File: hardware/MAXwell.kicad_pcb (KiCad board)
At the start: 2 copper layers, 155 parts, among them J1 Conn_02x05_Odd_Even, J2 Conn_02x12_Counter_Clockwise, J3 Barrel_Jack_Switch_Pin3Ring, SW1 SW_Push_Dual, SW10 SW_Wuerth_450301014042, SW11 SW_Wuerth_450301014042, SW12 SW_Wuerth_450301014042, SW13 SW_Wuerth_450301014042, SW2 SW_Push_Dual, SW3 SW_Push_Dual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

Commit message: started routing
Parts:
- SW1, SW2, SW3, SW4: footprint Button_Switch_THT:SW_PUSH-12mm -> Library:SW_PUSH-12mm
- moved D1 125.7 mm to (236.7, 131.5)
- moved D14 125.7 mm to (246.3, 134.5)
- moved D15 125.7 mm to (246.3, 137.5)
- moved D16 125.7 mm to (246.3, 140.6)
- moved D2 125.7 mm to (236.7, 134.5)
- moved D3 125.7 mm to (236.7, 137.5)
- moved D4 125.7 mm to (236.7, 140.6)
- moved D5 125.7 mm to (236.7, 143.6)
- moved R1 125.4 mm to (260.4, 109.3)
- moved R2 125.4 mm to (260.4, 112.2)
- moved R3 125.4 mm to (260.4, 115.2)
- moved R5 125.4 mm to (260.4, 121.1)
- moved R4 125.4 mm to (260.4, 118.1)
- moved R62 116.8 mm to (273.8, 128.0)
- moved R63 116.8 mm to (273.8, 130.9)
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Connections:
- J2 pad 2: +3V3 -> GND
- J2 pad 21: GND -> Net-(J2-Pin_21)
- J2 pad 22: GND -> Net-(J2-Pin_22)
- J2 pad 23: GND -> Net-(J2-Pin_23)
- J2 pad 24: GND -> Net-(J2-Pin_24)
- J2 pad 3: Net-(J2-Pin_3) -> +3V3
- J2 pad 4: Net-(J2-Pin_4) -> GND
- J2 pad 6: Net-(J2-Pin_6) -> GND
- J2 pad 8: Net-(J2-Pin_8) -> GND
- U5 pad 62: Net-(J2-Pin_3) -> Net-(J2-Pin_5)
- U5 pad 64: Net-(J2-Pin_4) -> Net-(J2-Pin_7)
- U5 pad 66: Net-(J2-Pin_5) -> Net-(J2-Pin_9)
- U5 pad 67: Net-(J2-Pin_6) -> Net-(J2-Pin_11)
- U5 pad 68: Net-(J2-Pin_7) -> Net-(J2-Pin_13)
- U5 pad 69: Net-(J2-Pin_8) -> Net-(J2-Pin_15)
- U5 pad 70: Net-(J2-Pin_9) -> Net-(J2-Pin_17)
- U5 pad 71: Net-(J2-Pin_10) -> Net-(J2-Pin_19)
- U5 pad 72: Net-(J2-Pin_11) -> Net-(J2-Pin_21)
- U5 pad 73: Net-(J2-Pin_12) -> Net-(J2-Pin_23)
- U5 pad 74: Net-(J2-Pin_13) -> Net-(J2-Pin_24)
- U5 pad 75: Net-(J2-Pin_14) -> Net-(J2-Pin_22)
- U5 pad 76: Net-(J2-Pin_15) -> Net-(J2-Pin_20)
- U5 pad 77: Net-(J2-Pin_16) -> Net-(J2-Pin_18)
- U5 pad 78: Net-(J2-Pin_17) -> Net-(J2-Pin_16)
- U5 pad 81: Net-(J2-Pin_18) -> Net-(J2-Pin_14)
- U5 pad 82: Net-(J2-Pin_19) -> Net-(J2-Pin_12)
- U5 pad 83: Net-(J2-Pin_20) -> Net-(J2-Pin_10)
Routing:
- net +3V3: track 0.00 -> 110.3 mm
- net Net-(R45-Pad2): track 0.00 -> 18.3 mm
- net Net-(R50-Pad2): track 0.00 -> 18.3 mm
- net Net-(R42-Pad2): track 0.00 -> 18.2 mm
- net Net-(R48-Pad2): track 0.00 -> 18.2 mm
- net Net-(U5-IO1_12/GCLK0): track 0.00 -> 17.1 mm
- net Net-(R47-Pad1): track 0.00 -> 16.7 mm
- net Net-(R44-Pad1): track 0.00 -> 16.7 mm
- net Net-(R61-Pad1): track 0.00 -> 16.6 mm
- net Net-(R60-Pad1): track 0.00 -> 16.6 mm
- net Net-(SW11-C): track 0.00 -> 13.5 mm
- net Net-(SW10-C): track 0.00 -> 13.5 mm
- net Net-(SW8-C): track 0.00 -> 13.5 mm
- net Net-(SW7-C): track 0.00 -> 13.5 mm
- net Net-(SW6-C): track 0.00 -> 13.5 mm
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
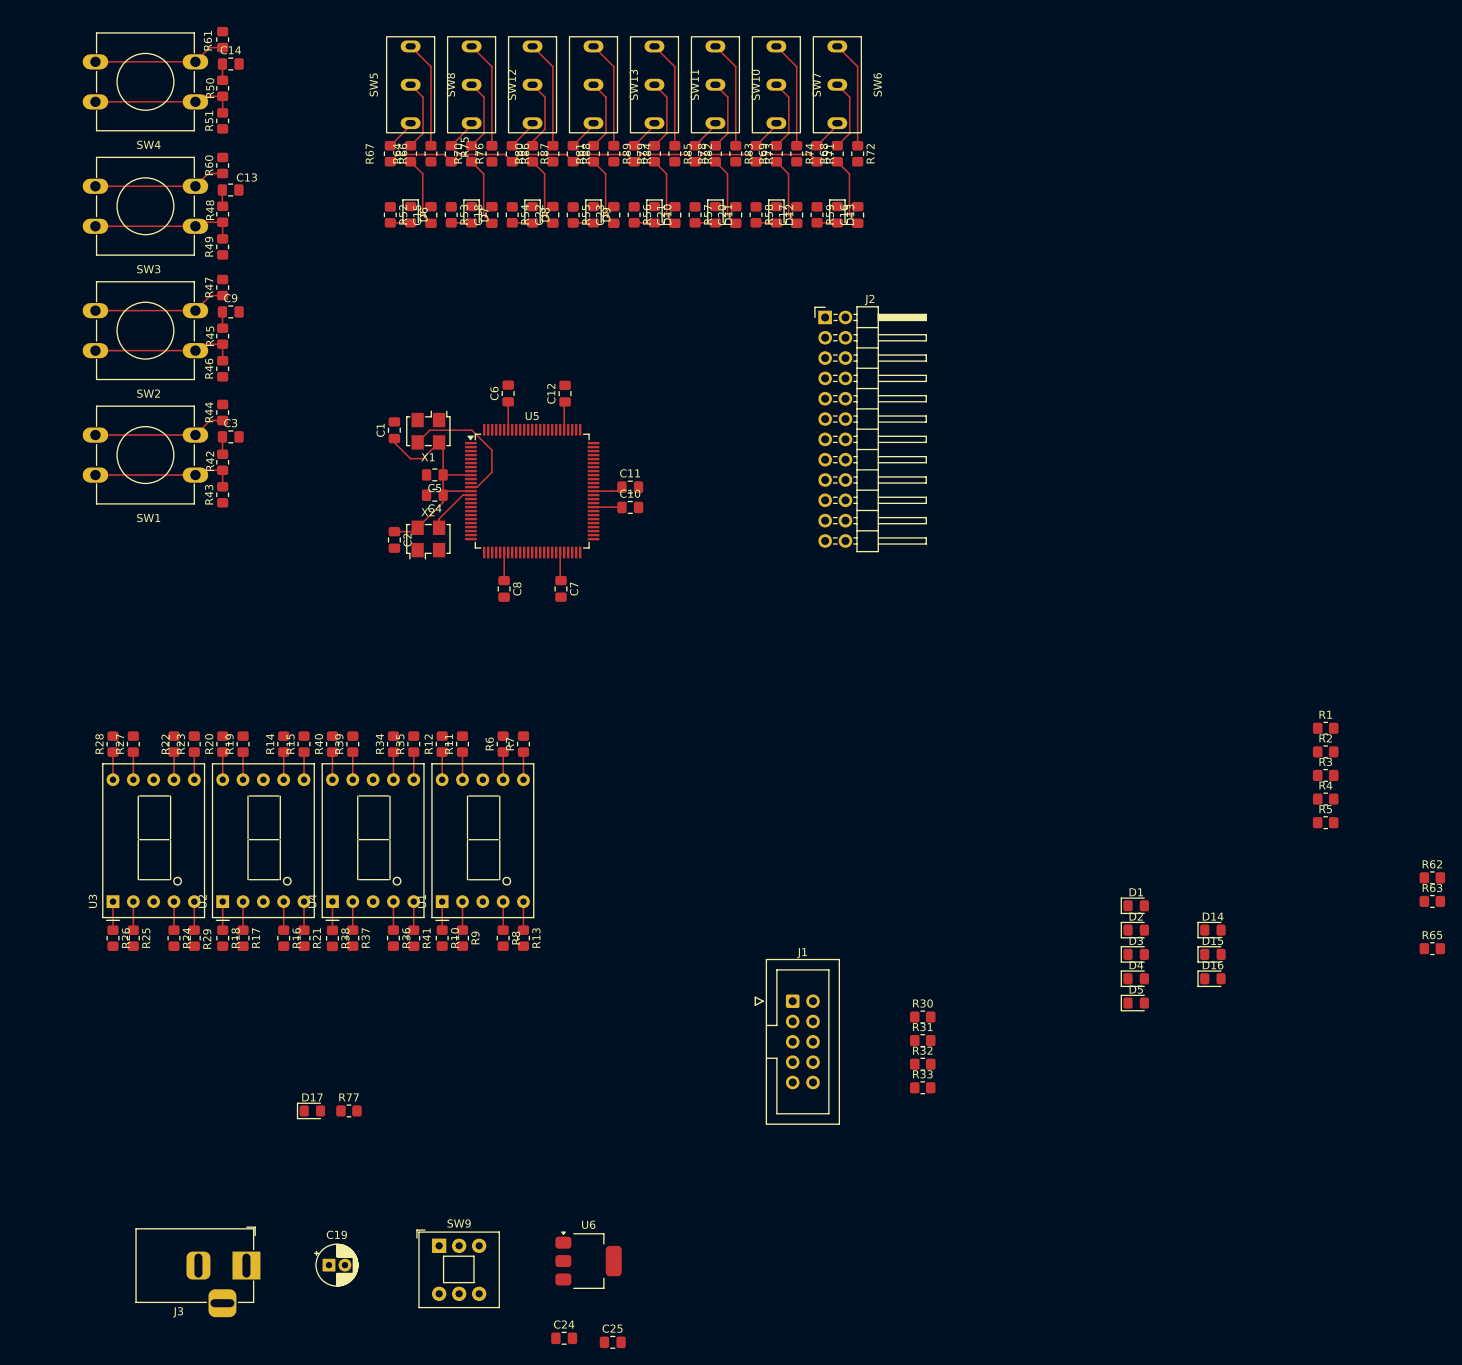
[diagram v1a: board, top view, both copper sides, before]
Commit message: pcb outline defined, ready for autorouter test
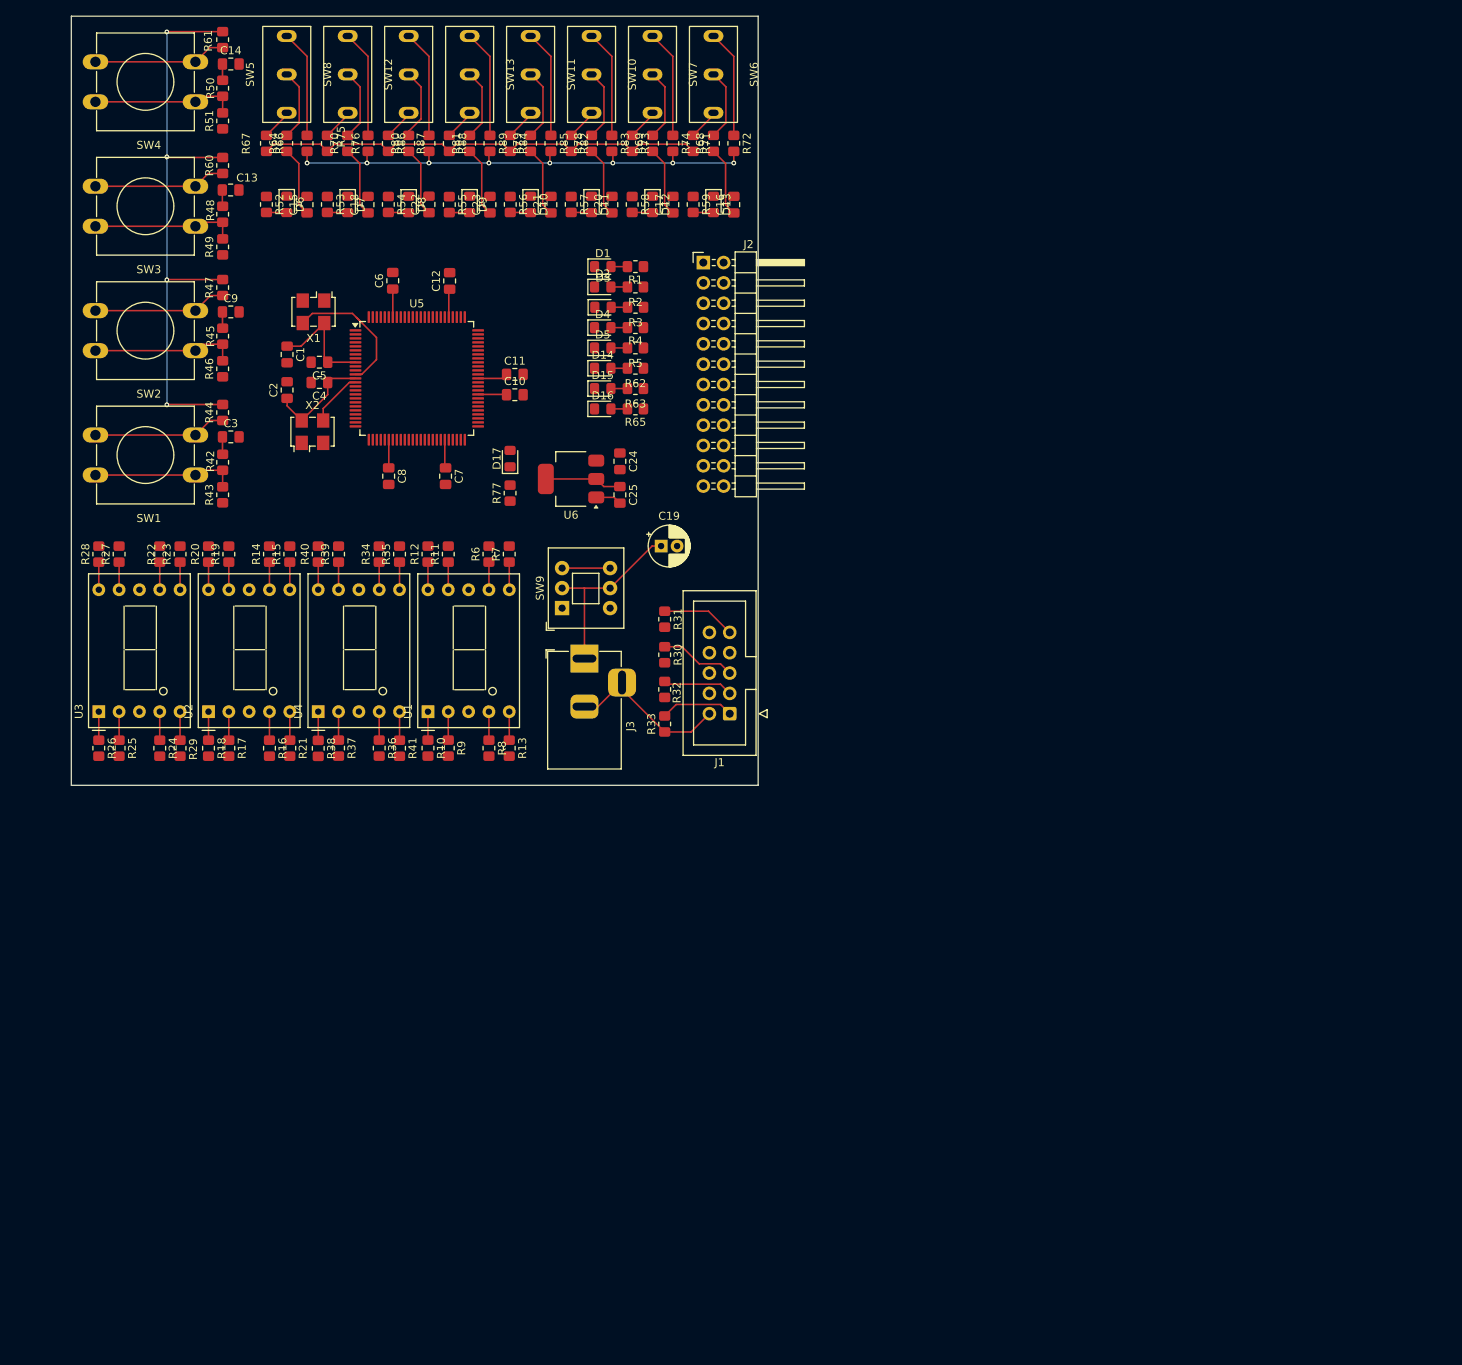
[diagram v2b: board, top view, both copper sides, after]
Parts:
- moved R65 120.3 mm to (174.1, 69.3), turned to 180 degrees
- moved R63 118.5 mm to (174.1, 66.8), turned to 180 degrees
- moved R62 118.2 mm to (174.1, 64.3), turned to 180 degrees
- moved C24 109.8 mm to (172.2, 75.9), turned to -90 degrees
- moved C25 105.9 mm to (172.2, 80.1), turned to -90 degrees
- moved D5 105.6 mm to (170.1, 61.7)
- moved D4 105.2 mm to (170.1, 59.2)
- moved D3 104.8 mm to (170.1, 56.6)
- moved R5 104.7 mm to (174.1, 61.7), turned to 180 degrees
- moved R4 104.5 mm to (174.1, 59.2), turned to 180 degrees
- moved D2 104.4 mm to (170.1, 54.1)
- moved D16 104.4 mm to (170.1, 69.3)
- moved R3 104.2 mm to (174.2, 56.6), turned to 180 degrees
- moved D1 104.1 mm to (170.1, 51.6)
- moved R2 104.0 mm to (174.1, 54.1), turned to 180 degrees
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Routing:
- net GND: track 0.00 -> 89.3 mm, vias 0 -> 8
- net +3V3: track 110.3 -> 192.0 mm, vias 0 -> 4
- net Net-(C19-Pad1): track 0.00 -> 23.4 mm
- net Net-(J1-Pin_5): track 0.00 -> 9.49 mm
- net Net-(J1-Pin_9): track 0.00 -> 9.23 mm
- net Net-(J1-Pin_1): track 0.00 -> 9.20 mm
- net Net-(J1-Pin_3): track 0.00 -> 8.75 mm
- net +5V: track 0.00 -> 6.04 mm
- net Net-(D5-A): track 0.00 -> 2.06 mm
- net Net-(D4-A): track 0.00 -> 2.06 mm
- net Net-(D2-A): track 0.00 -> 2.06 mm
- net Net-(D16-A): track 0.00 -> 2.06 mm
- net Net-(D15-A): track 0.00 -> 2.06 mm
- net Net-(D14-A): track 0.00 -> 2.06 mm
- net Net-(D1-A): track 0.00 -> 2.06 mm
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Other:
- board outline added: 85.9 x 96.1 mm

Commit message: partially done 1/4
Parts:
- moved D1 19.1 mm to (174.8, 70.1), turned to 180 degrees
- moved R1 18.9 mm to (170.7, 70.1), turned to 0 degrees
- moved D16 17.7 mm to (174.8, 52.3), turned to 180 degrees
- moved R65 17.4 mm to (170.7, 52.3), turned to 0 degrees
- moved D2 14.3 mm to (174.8, 67.6), turned to 180 degrees
- moved R2 13.9 mm to (170.7, 67.6), turned to 0 degrees
- moved D15 12.8 mm to (174.8, 54.9), turned to 180 degrees
- moved R63 12.4 mm to (170.7, 54.9), turned to 0 degrees
- moved D3 9.60 mm to (174.8, 65.0), turned to 180 degrees
- moved R3 9.07 mm to (170.7, 65.0), turned to 0 degrees
- moved D14 8.34 mm to (174.8, 57.4), turned to 180 degrees
- moved R62 7.67 mm to (170.7, 57.4), turned to 0 degrees
- moved D4 5.78 mm to (174.8, 62.5), turned to 180 degrees
- moved D5 5.06 mm to (174.8, 59.9), turned to 180 degrees
- moved R4 4.77 mm to (170.7, 62.5), turned to 0 degrees
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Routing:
- net GND: track 89.3 -> 285.8 mm
- net Net-(U5-IO2_87): track 8.75 -> 57.4 mm
- net Net-(U5-IO2_88): track 8.75 -> 50.6 mm
- net Net-(U5-IO1_50): track 0.00 -> 36.7 mm
- net Net-(U5-IO2_89): track 8.75 -> 43.8 mm
- net Net-(U5-IO2_84): track 0.00 -> 32.7 mm
- net Net-(J2-Pin_7): track 0.00 -> 32.3 mm, vias 0 -> 1
- net Net-(U5-IO2_85): track 0.00 -> 32.0 mm
- net Net-(U5-IO1_51): track 0.00 -> 31.9 mm
- net Net-(U5-IO2_86): track 0.00 -> 31.2 mm
- net +3V3: track 192.0 -> 221.9 mm, vias 4 -> 6
- net Net-(J2-Pin_11): track 0.00 -> 29.7 mm, vias 0 -> 1
- net Net-(J2-Pin_9): track 0.00 -> 29.3 mm, vias 0 -> 2
- net Net-(U5-IO2_90): track 8.75 -> 36.9 mm
- net Net-(U5-IO1_49): track 0.00 -> 22.1 mm
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
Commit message: nearly done
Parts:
- moved X2 1.75 mm to (132.1, 72.6)
- moved R9 1.14 mm to (151.9, 111.8)
- moved R25 1.14 mm to (110.7, 111.8)
- moved R37 1.14 mm to (138.2, 111.7)
- moved R77 0.90 mm to (158.5, 80.8)
- moved R24 0.89 mm to (113.8, 111.8)
- moved R34 0.89 mm to (141.2, 87.5)
- moved R36 0.89 mm to (141.2, 111.7)
- moved R6 0.89 mm to (154.9, 87.5)
- moved R8 0.89 mm to (154.9, 111.8)
- moved R14 0.89 mm to (127.5, 87.5)
- moved R16 0.89 mm to (127.5, 111.8)
- moved R22 0.89 mm to (113.8, 87.5)
- moved D17 0.64 mm to (158.5, 76.2)
- moved R39 0.64 mm to (137.7, 87.5)
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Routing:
- net GND: track 285.8 -> 807.8 mm, vias 8 -> 24
- net +3V3: track 221.9 -> 424.0 mm, vias 6 -> 20
- net +5V: track 9.39 -> 88.3 mm, vias 0 -> 3
- net Net-(J1-Pin_1): track 9.20 -> 76.5 mm, vias 0 -> 4
- net Net-(J1-Pin_3): track 8.75 -> 75.4 mm, vias 0 -> 2
- net Net-(J1-Pin_5): track 9.49 -> 74.7 mm, vias 0 -> 8
- net Net-(U5-IO1_19): track 0.00 -> 63.7 mm, vias 0 -> 6
- net Net-(J2-Pin_20): track 0.00 -> 59.5 mm, vias 0 -> 1
- net Net-(U5-IO2_61): track 0.00 -> 57.8 mm, vias 0 -> 8
- net Net-(J1-Pin_9): track 9.23 -> 66.7 mm, vias 0 -> 2
- net Net-(U5-IO1_29): track 0.00 -> 55.9 mm, vias 0 -> 2
- net Net-(J2-Pin_22): track 0.00 -> 55.6 mm, vias 0 -> 1
- net Net-(J2-Pin_12): track 0.00 -> 53.8 mm, vias 0 -> 3
- net Net-(J2-Pin_10): track 0.00 -> 53.2 mm, vias 0 -> 2
- net Net-(U5-IO1_39): track 0.00 -> 49.4 mm
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
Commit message: last attempt to autorouter
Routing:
- net Net-(U5-IO1_18): track 0.00 -> 56.5 mm
- net Net-(U5-IO1_17): track 0.00 -> 53.8 mm
- net Net-(U5-IO1_21): track 0.00 -> 33.7 mm, vias 0 -> 2
- net Net-(U5-IO1_15): track 0.00 -> 25.2 mm
- net Net-(U5-IO1_16): track 0.00 -> 23.3 mm, vias 0 -> 2

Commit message: routing done
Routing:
- net Net-(U5-IO1_5): track 0.00 -> 74.7 mm, vias 0 -> 2
- net Net-(U5-IO1_3): track 0.00 -> 73.8 mm, vias 0 -> 4
- net Net-(U5-IO1_4): track 0.00 -> 71.7 mm, vias 0 -> 2
- net Net-(U5-IO1_8): track 0.00 -> 65.1 mm, vias 0 -> 2
- net GND: track 807.8 -> 861.0 mm, vias 24 -> 28
- net Net-(U5-IO2_1): track 0.00 -> 43.1 mm, vias 0 -> 4
- net Net-(U5-IO1_2): track 0.00 -> 40.7 mm, vias 0 -> 4
- net +3V3: track 424.0 -> 438.7 mm, vias 20 -> 22
- net Net-(U5-IO1_12/GCLK0): track 16.9 -> 22.7 mm

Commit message: cleanup pcb design
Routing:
- net +3V3: track 438.7 -> 431.7 mm
- net GND: track 861.0 -> 857.3 mm
- net Net-(J1-Pin_3): track 75.4 -> 74.2 mm
- net Net-(R45-Pad2): track 18.3 -> 17.2 mm
- net Net-(R50-Pad2): track 18.3 -> 17.3 mm
- net Net-(R42-Pad2): track 18.2 -> 17.4 mm
- net Net-(R48-Pad2): track 18.2 -> 17.5 mm
- net Net-(J2-Pin_5): track 34.0 -> 33.5 mm
- net Net-(J2-Pin_11): track 31.1 -> 30.6 mm

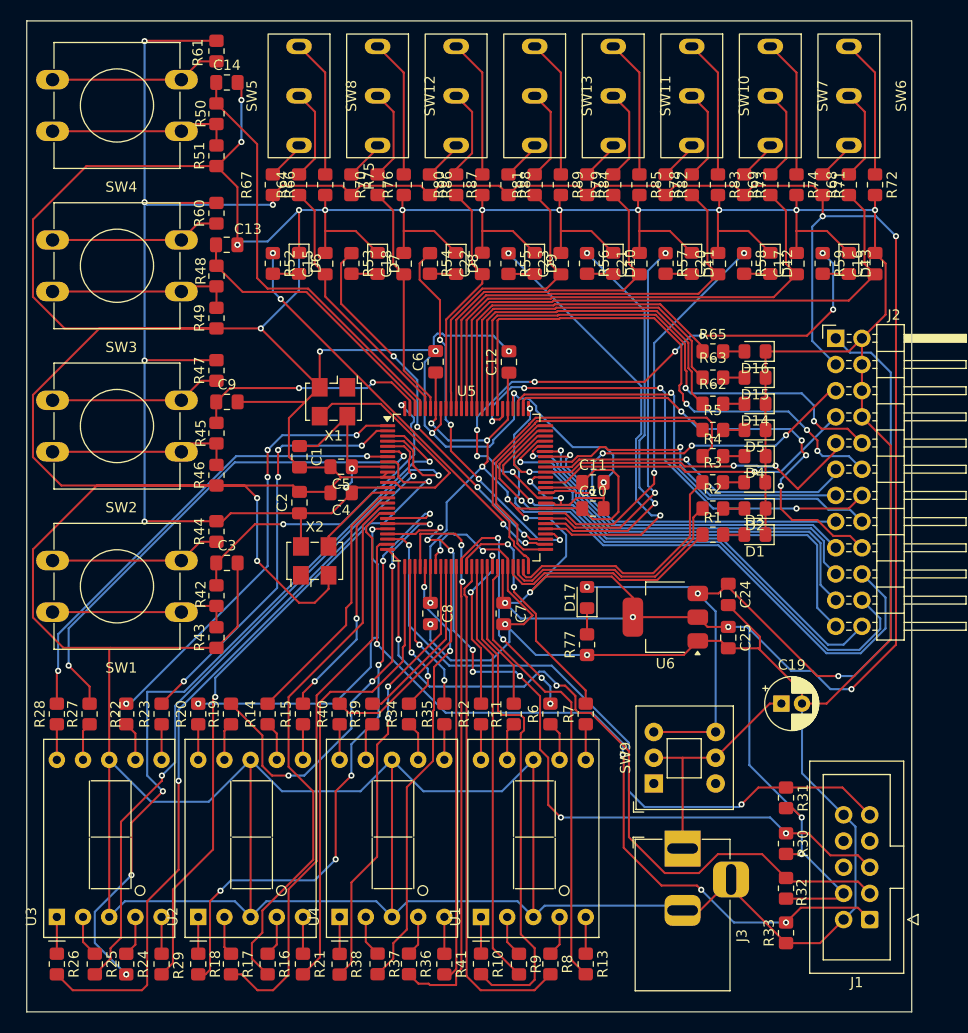
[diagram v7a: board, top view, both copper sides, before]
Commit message: replaced GND traces on backside with ground plane
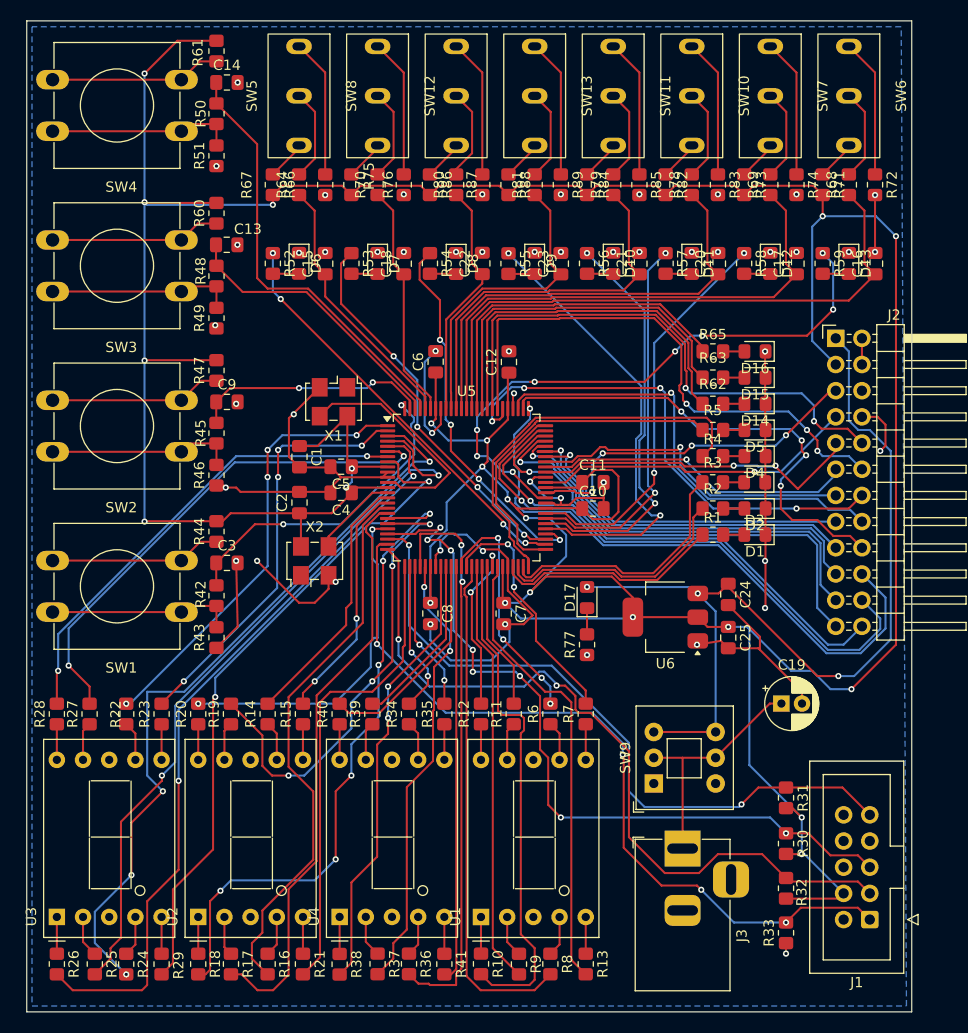
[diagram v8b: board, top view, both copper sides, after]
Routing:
- net GND: track 857.3 -> 170.2 mm, vias 28 -> 52
- net +3V3: track 431.7 -> 429.8 mm
- net +5V: track 87.9 -> 87.4 mm
- added copper zone on B.Cu, net GND
